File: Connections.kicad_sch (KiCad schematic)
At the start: 19 parts, among them J500 Debug, J501 UART, J502 I2C, J503 CAN port, J504 Motor, J505 Gimbal, J506 USB C, U500 MCP2562T-E_SN

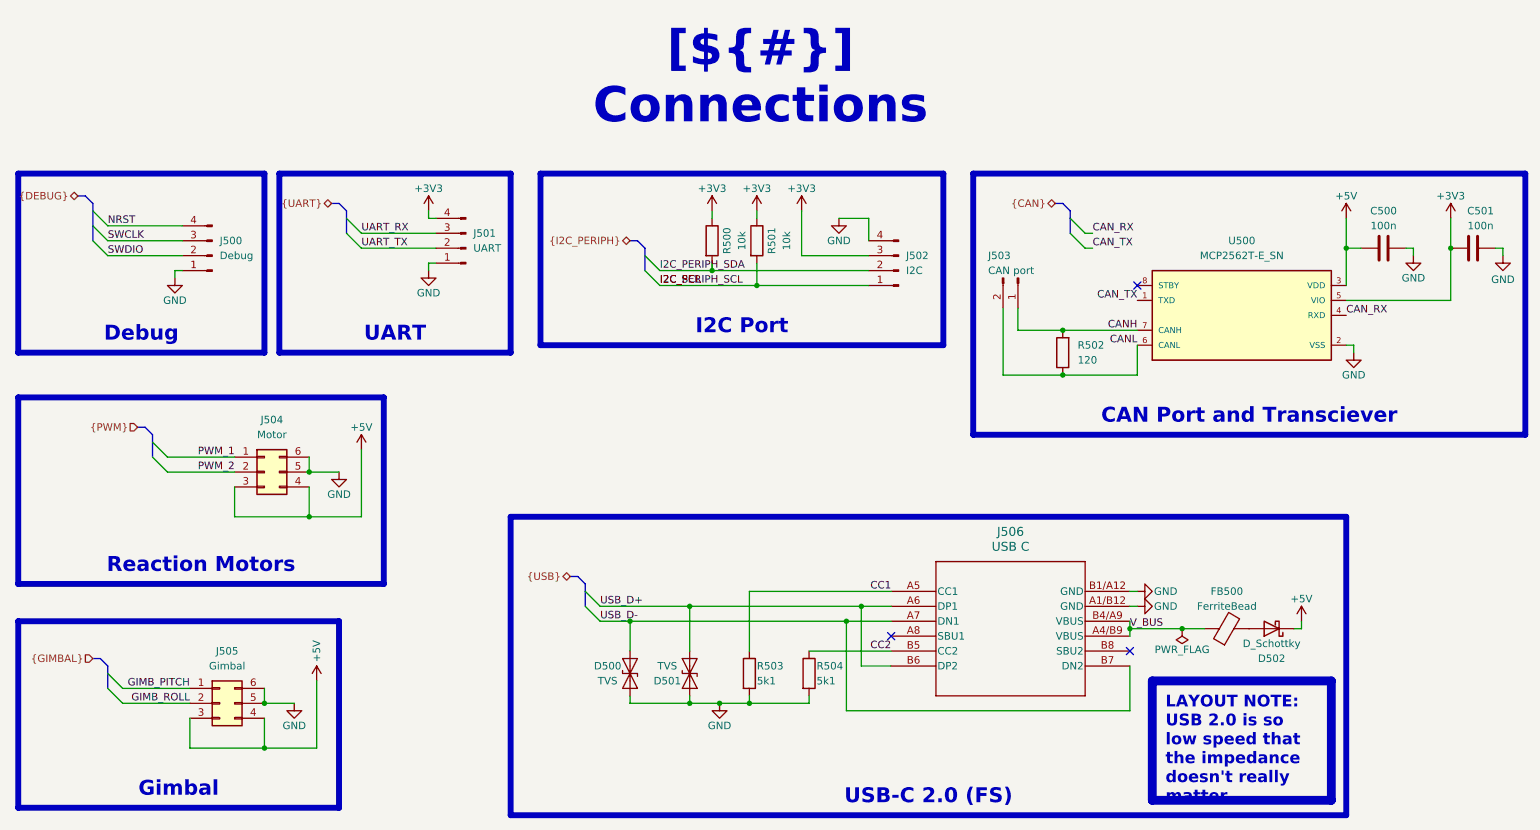
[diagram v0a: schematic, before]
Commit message: [PCB][Fixed] Fixed wrong Diode footprint and Changed TVS diode package, also changed wrong footprint of CAN transiever chip. [Changed] Changed the FLASH chip to a different model due to a stocking issue
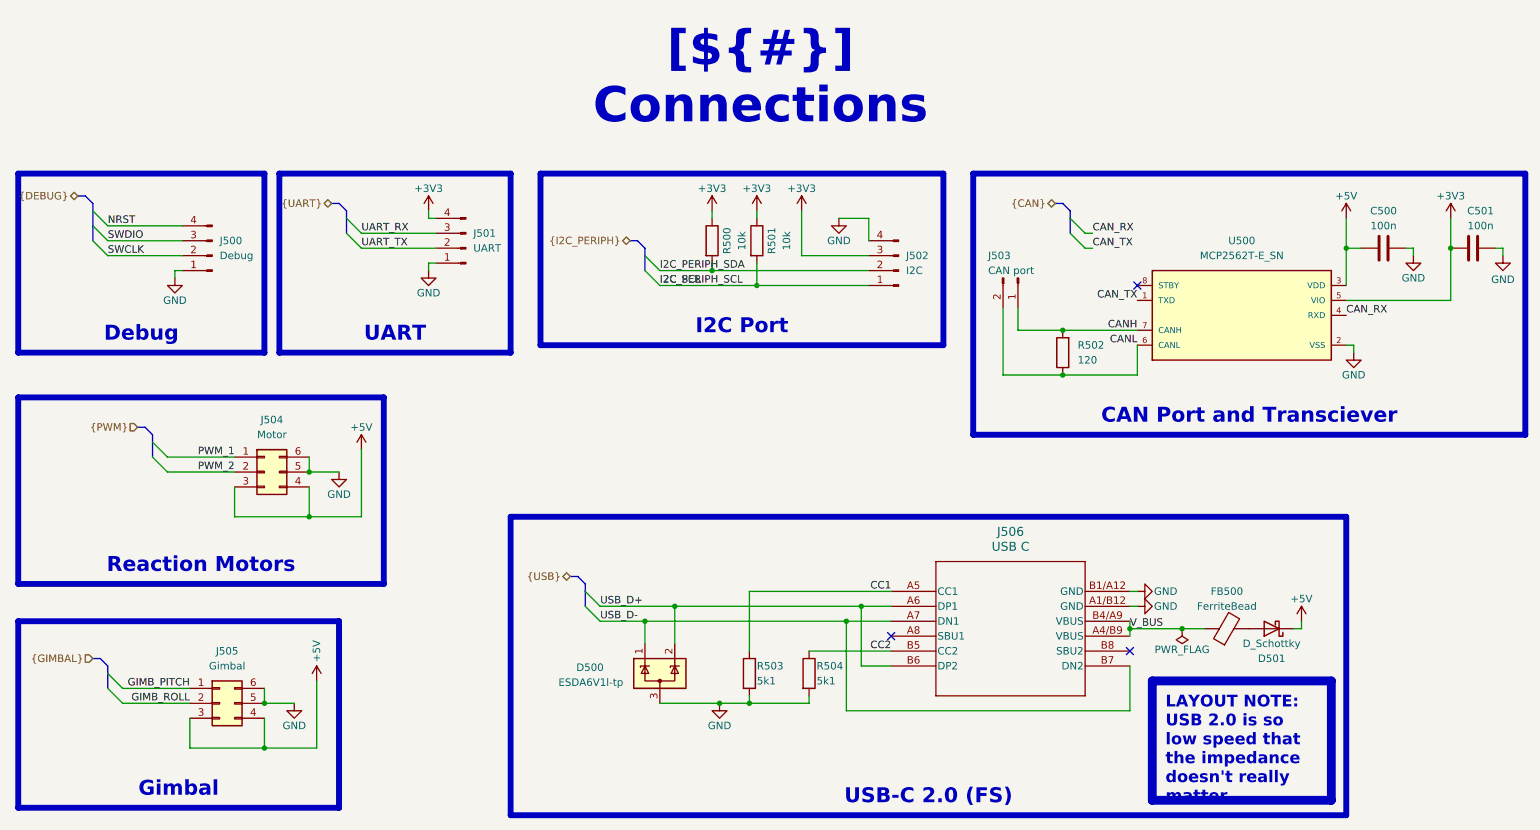
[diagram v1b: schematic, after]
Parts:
- removed D500, D501: TVS, Diode_SMD:D_SOD-323F, symbol Diode:ESD131-B1-W0201
- added D500: ESDA6V1l-tp, Package_TO_SOT_SMD:SOT-23-3, symbol Power_Protection:ESDA5V3L
- D501: renamed from D502; footprint Diode_SMD:D_0805_2012Metric -> DO214AAC:P25_DO-214AC_SMA
- U500: footprint Package_SO:SOIC-8_5.3x5.3mm_P1.27mm -> Package_SO:SOIC-8_3.9x4.9mm_P1.27mm
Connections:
- net GND: now also D500.3 (A)
- net SWCLK: now also J500.2 (Pin_2); no longer J500.3 (Pin_3)
- net SWDIO: now also J500.3 (Pin_3); no longer J500.2 (Pin_2)
- net USB_D+: now also D500.2 (K)
- net USB_D-: now also D500.1 (K)
